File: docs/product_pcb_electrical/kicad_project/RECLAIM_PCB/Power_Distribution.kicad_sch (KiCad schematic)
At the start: 37 parts, among them J1 Conn_01x02, K1 G5LE-1, K1 G5LE-1A-DC24, Q1 2N7002, Q1 IRLZ44N, SW1 SW_Push, U1 LM5116SD, U2 TPS5430DDA, U3 AMS1117-3.3

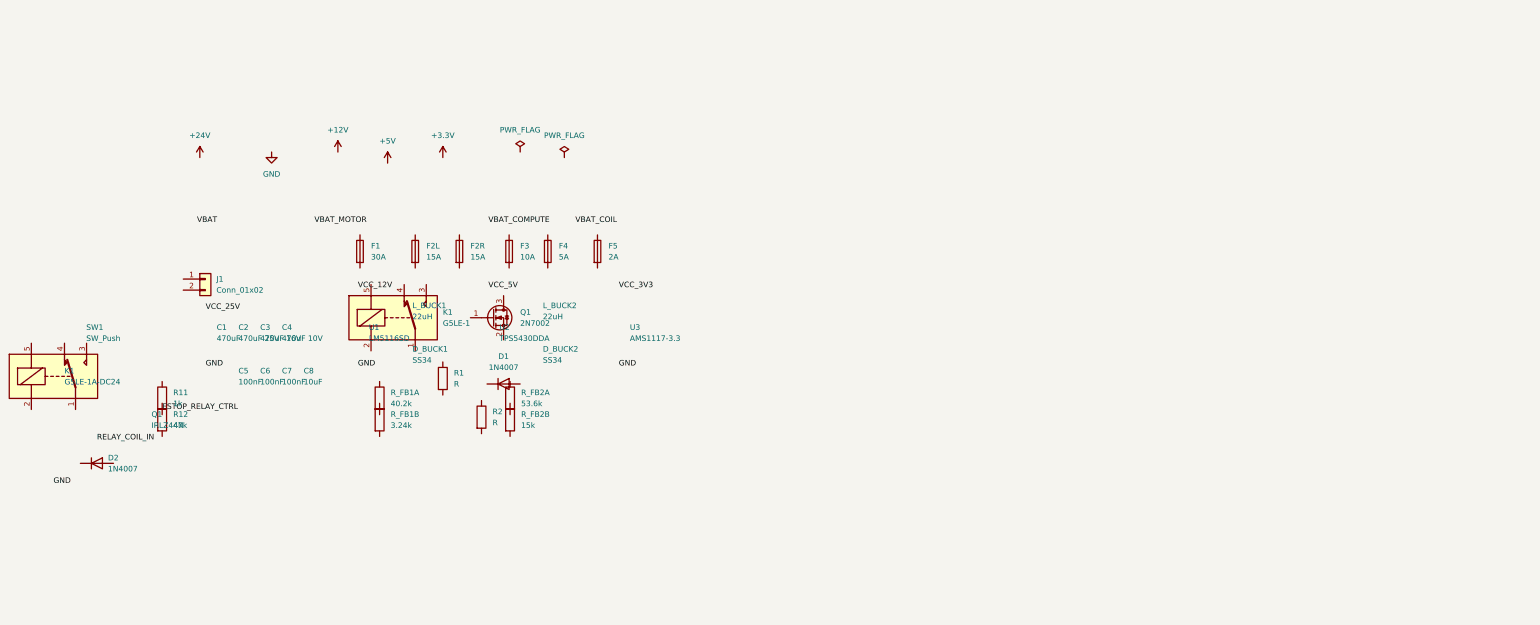
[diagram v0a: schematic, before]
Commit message: Add prototype schematic + tighten product layout to A3
Product: All 4 sub-sheets resized A2/A1→A3, components repositioned
into tight logical groups, duplicate K1/Q1 removed.

Prototype: New KiCad project with 3 hierarchical sheets
(Power, Teensy/Motor Control, Peripherals/Sensors), BOM, and
netlist reflecting as-built wiring: MD13C R3 + BTS7960 asymmetric
drivers, DC disconnect, 6-way fuse block, XINGYHENG servo buck.

Co-Authored-By: Claude Opus 4.6 <noreply@anthropic.com>
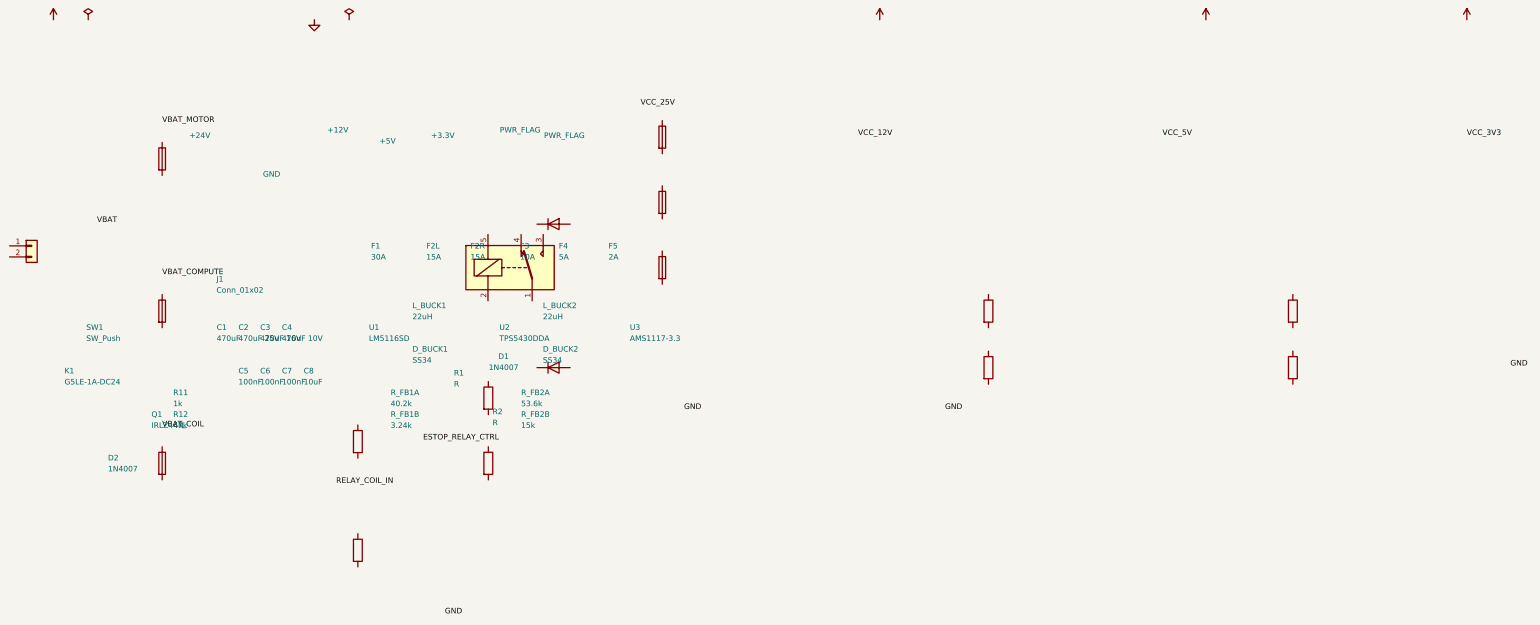
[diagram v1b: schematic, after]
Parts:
- removed K1: G5LE-1, Relay_THT:Relay_SPDT_Omron-G5LE-1, symbol Relay:G5LE-1
- removed Q1: 2N7002, Package_TO_SOT_SMD:SOT-23, symbol Transistor_FET:2N7002
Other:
- moved on the sheet: D1, D2, F1, F2L, F2R, F3, F4, F5, J1, K1, R1, R11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
